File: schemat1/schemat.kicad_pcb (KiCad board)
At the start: 2 copper layers, 100 x 100 mm, 91 parts, among them J1 Light Test Bridge, J2 Power Pins, Q1 BC547, Q2 BC547, Q3 BC547, Q4 BC547, Q5 NMOS, SW1 Player 1, SW2 Player 2, SW3 SW_Push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

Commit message: zmiana elementu C7 na elektrolityczny, aktualizacja w schemacie i na pcb
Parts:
- C7: value 10n -> 100u; footprint Capacitor_THT:C_Disc_D3.4mm_W2.1mm_P2.50mm -> Capacitor_THT:CP_Radial_D6.3mm_P2.50mm
- moved R9 4.45 mm to (33.4, 108.0)
- moved R15 4.25 mm to (33.3, 103.2)
- moved R13 2.55 mm to (33.3, 98.4)
- moved R11 1.85 mm to (33.4, 92.6)
- moved C7 1.77 mm to (41.0, 114.0), turned to 0 degrees
- moved TP9 1.75 mm to (48.0, 117.5)
- moved R8 0.15 mm to (33.4, 87.8)
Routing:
- net Net-(U5-DIS): track 21.0 -> 27.2 mm
- net Net-(Q4-C): track 3.45 -> 5.57 mm
- net Net-(Q3-C): track 3.53 -> 4.85 mm
- net Net-(Q2-C): track 3.45 -> 4.48 mm
- net Net-(Q1-E): track 38.8 -> 38.1 mm
- net Net-(Q1-C): track 3.45 -> 4.02 mm

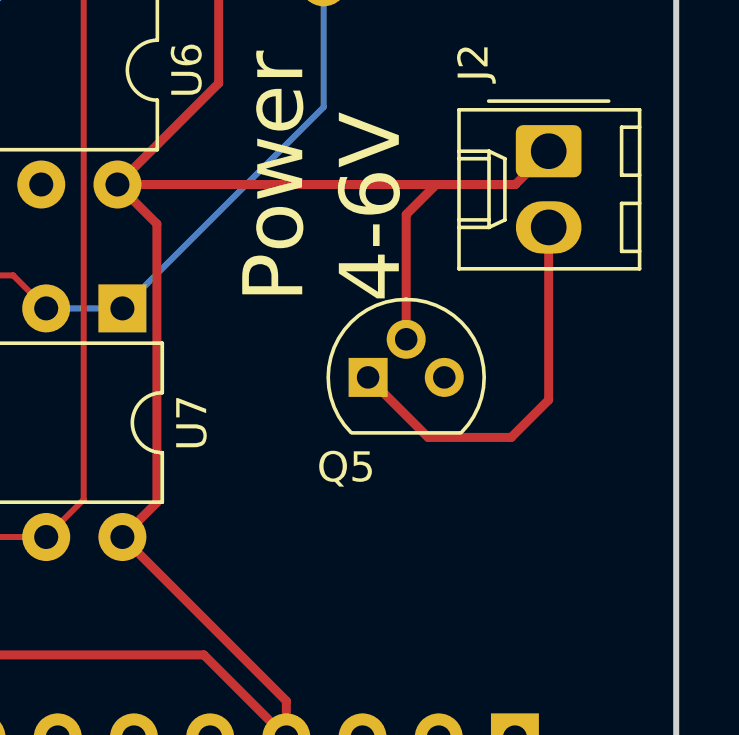
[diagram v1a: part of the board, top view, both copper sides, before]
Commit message: zmiana footprinta tranzystora w układzie zabezpieczającym przed przeciwną polaryzacją
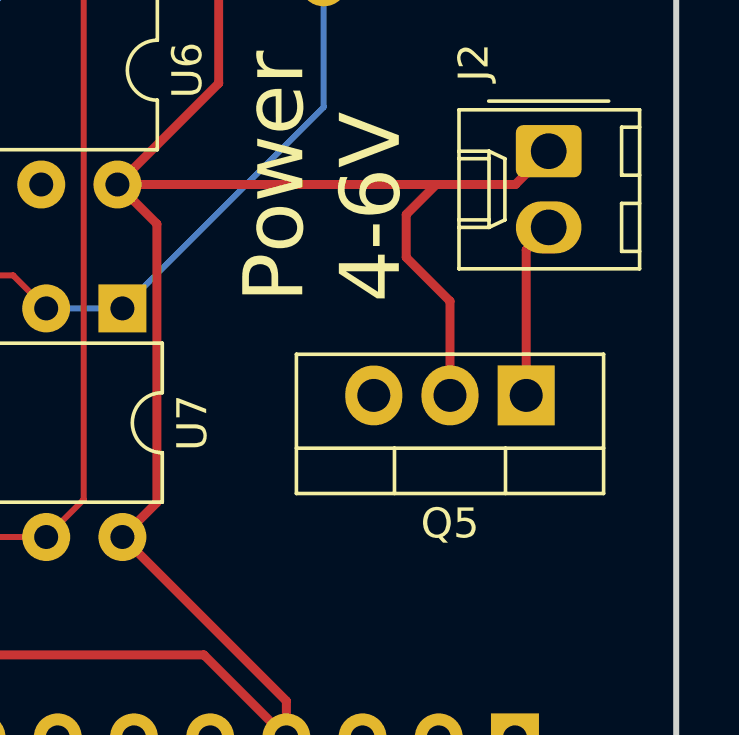
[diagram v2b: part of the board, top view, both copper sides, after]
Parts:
- Q5: footprint Package_TO_SOT_THT:TO-92 -> Package_TO_SOT_THT:TO-220-3_Vertical
- moved Q5 5.30 mm to (115.0, 60.6), turned to 180 degrees
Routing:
- net Net-(J2-Pin_2): track 13.8 -> 6.62 mm
- net +5V: track 369.7 -> 372.2 mm
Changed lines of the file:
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@@
 		)
 	)
-	(footprint "Package_TO_SOT_THT:TO-92"
+	(footprint "Package_TO_SOT_THT:TO-220-3_Vertical"
 		(layer "F.Cu")
-		(at 109.73 60)
-		(descr "TO-92 leads molded, narrow, drill 0.75mm (see NXP sot054_po.pdf)")
-		(tags "to-92 sc-43 sc-43a sot54 PA33 transistor")
+		(at 115 60.6 180)
+		(descr "TO-220-3, Vertical, RM 2.54mm, see https://www.vishay.com/docs/66542/to-220-1.pdf")
+		(tags "TO-220-3 Vertical RM 2.54mm")
 		(property "Reference" "Q5"
-			(at -0.73 3 0)
+			(at 2.54 -4.27 180)
 			(layer "F.SilkS")
 			(effects
@@
 		)
 		(property "Value" "NMOS"
-			(at 1.27 2.79 0)
+			(at 2.54 2.5 180)
 			(layer "F.Fab")
 			(effects
@@
 			)
 		)
-		(property "Footprint" "Package_TO_SOT_THT:TO-92"
-			(at 0 0 0)
+		(property "Footprint" "Package_TO_SOT_THT:TO-220-3_Vertical"
+			(at 0 0 180)
 			(unlocked yes)
 			(layer "F.Fab")
@@
 		)
 		(property "Datasheet" "https://ngspice.sourceforge.io/docs/ngspice-html-manual/manual.xhtml#cha_MOSFETs"
-			(at 0 0 0)
+			(at 0 0 180)
 			(unlocked yes)
 			(layer "F.Fab")
@@
 		)
 		(property "Description" "N-MOSFET transistor, drain/source/gate"
-			(at 0 0 0)
+			(at 0 0 180)
 			(unlocked yes)
 			(layer "F.Fab")
@@
 		)
 		(property "Sim.Device" "NMOS"
-			(at 0 0 0)
+			(at 0 0 180)
 			(unlocked yes)
 			(layer "F.Fab")
@@
 		)
 		(property "Sim.Type" "VDMOS"
-			(at 0 0 0)
+			(at 0 0 180)
 			(unlocked yes)
 			(layer "F.Fab")
@@
 		)
 		(property "Sim.Pins" "1=D 2=G 3=S"
-			(at 0 0 0)
+			(at 0 0 180)
 			(unlocked yes)
 			(layer "F.Fab")
@@
 		(attr through_hole)
 		(fp_line
-			(start -0.53 1.85)
-			(end 3.07 1.85)
+			(start 7.66 -3.27)
+			(end 7.66 1.371)
 			(stroke
 				(width 0.12)
@@
 			(layer "F.SilkS")
 		)
-		(fp_arc
-			(start -0.568478 1.838478)
-			(mid -1.132087 -0.994977)
-			(end 1.27 -2.6)
+		(fp_line
+			(start 4.391 -3.27)
+			(end 4.391 -1.76)
 			(stroke
 				(width 0.12)
@@
 			(layer "F.SilkS")
 		)
-		(fp_arc
-			(start 1.27 -2.6)
-			(mid 3.672087 -0.994977)
-			(end 3.108478 1.838478)
+		(fp_line
+			(start 0.69 -3.27)
+			(end 0.69 -1.76)
 			(stroke
 				(width 0.12)
@@
 		)
 		(fp_line
-			(start -1.46 -2.73)
-			(end -1.46 2.01)
+			(start -2.58 1.371)
+			(end 7.66 1.371)
+			(stroke
+				(width 0.12)
+				(type solid)
+			)
+			(layer "F.SilkS")
+		)
+		(fp_line
+			(start -2.58 -1.76)
+			(end 7.66 -1.76)
+			(stroke
+				(width 0.12)
+				(type solid)
+			)
+			(layer "F.SilkS")
+		)
+		(fp_line
+			(start -2.58 -3.27)
+			(end 7.66 -3.27)
+			(stroke
+				(width 0.12)
+				(type solid)
+			)
+			(layer "F.SilkS")
+		)
+		(fp_line
+			(start -2.58 -3.27)
+			(end -2.58 1.371)
+			(stroke
+				(width 0.12)
+				(type solid)
+			)
+			(layer "F.SilkS")
+		)
+		(fp_line
+			(start 7.79 1.51)
+			(end 7.79 -3.4)
 			(stroke
 				(width 0.05)
@@
 		)
 		(fp_line
-			(start -1.46 -2.73)
-			(end 4 -2.73)
+			(start 7.79 -3.4)
+			(end -2.71 -3.4)
 			(stroke
 				(width 0.05)
@@
 		)
 		(fp_line
-			(start 4 2.01)
-			(end -1.46 2.01)
+			(start -2.71 1.51)
+			(end 7.79 1.51)
 			(stroke
 				(width 0.05)
@@
 		)
 		(fp_line
-			(start 4 2.01)
-			(end 4 -2.73)
+			(start -2.71 -3.4)
+			(end -2.71 1.51)
 			(stroke
 				(width 0.05)
@@
 		)
 		(fp_line
-			(start -0.5 1.75)
-			(end 3 1.75)
+			(start 7.54 1.25)
+			(end 7.54 -3.15)
 			(stroke
 				(width 0.1)
@@
 			(layer "F.Fab")
 		)
-		(fp_arc
-			(start -0.483625 1.753625)
-			(mid -1.021221 -0.949055)
-			(end 1.27 -2.48)
+		(fp_line
+			(start 7.54 -3.15)
+			(end -2.46 -3.15)
 			(stroke
 				(width 0.1)
@@
 			(layer "F.Fab")
 		)
-		(fp_arc
-			(start 1.27 -2.48)
-			(mid 3.561221 -0.949055)
-			(end 3.023625 1.753625)
+		(fp_line
+			(start 4.39 -3.15)
+			(end 4.39 -1.88)
+			(stroke
+				(width 0.1)
+				(type solid)
+			)
+			(layer "F.Fab")
+		)
+		(fp_line
+			(start 0.69 -3.15)
+			(end 0.69 -1.88)
+			(stroke
+				(width 0.1)
+				(type solid)
+			)
+			(layer "F.Fab")
+		)
+		(fp_line
+			(start -2.46 1.25)
+			(end 7.54 1.25)
+			(stroke
+				(width 0.1)
+				(type solid)
+			)
+			(layer "F.Fab")
+		)
+		(fp_line
+			(start -2.46 -1.88)
+			(end 7.54 -1.88)
+			(stroke
+				(width 0.1)
+				(type solid)
+			)
+			(layer "F.Fab")
+		)
+		(fp_line
+			(start -2.46 -3.15)
+			(end -2.46 1.25)
 			(stroke
 				(width 0.1)
@@
 		)
 		(fp_text user "${REFERENCE}"
-			(at 1.27 0 0)
+			(at 2.54 -4.27 180)
 			(layer "F.Fab")
 			(effects
@@
 		)
 		(pad "1" thru_hole rect
-			(at 0 0)
-			(size 1.3 1.3)
-			(drill 0.75)
+			(at 0 0 180)
+			(size 1.905 2)
+			(drill 1.1)
 			(layers "*.Cu" "*.Mask")
 			(remove_unused_layers no)
@@
 			(pintype "passive")
 		)
-		(pad "2" thru_hole circle
-			(at 1.27 -1.27)
-			(size 1.3 1.3)
-			(drill 0.75)
+		(pad "2" thru_hole oval
+			(at 2.54 0 180)
+			(size 1.905 2)
+			(drill 1.1)
 			(layers "*.Cu" "*.Mask")
 			(remove_unused_layers no)
@@
 			(pintype "input")
 		)
-		(pad "3" thru_hole circle
-			(at 2.54 0)
-			(size 1.3 1.3)
-			(drill 0.75)
+		(pad "3" thru_hole oval
+			(at 5.08 0 180)
+			(size 1.905 2)
+			(drill 1.1)
 			(layers "*.Cu" "*.Mask")
 			(remove_unused_layers no)
@@
 			(pintype "passive")
 		)
-		(model "${KICAD8_3DMODEL_DIR}/Package_TO_SOT_THT.3dshapes/TO-92.wrl"
+		(model "${KICAD8_3DMODEL_DIR}/Package_TO_SOT_THT.3dshapes/TO-220-3_Vertical.wrl"
 			(offset
 				(xyz 0 0 0)
@@
 	)
 	(segment
-		(start 111 54.57)
-		(end 112 53.57)
-		(width 0.3)
-		(layer "F.Cu")
-		(net 2)
-	)
-	(segment
-		(start 111 54.57)
-		(end 111 58.73)
-		(width 0.3)
-		(layer "F.Cu")
-		(net 2)
-	)
-	(segment
 		(start 112 53.57)
 		(end 114.64 53.57)
@@
 	)
 	(segment
+		(start 111 54.57)
+		(end 111 56)
+		(width 0.3)
+		(layer "F.Cu")
+		(net 2)
+	)
+	(segment
 		(start 74.68 71.56)
 		(end 79.38 76.26)
@@
 	)
 	(segment
+		(start 112 53.57)
+		(end 111 54.57)
+		(width 0.3)
+		(layer "F.Cu")
+		(net 2)
+	)
+	(segment
 		(start 104.75 50.195)
 		(end 101.375 53.57)
@@
 	)
 	(segment
+		(start 112.46 57.46)
+		(end 112.46 60.6)
+		(width 0.3)
+		(layer "F.Cu")
+		(net 2)
+	)
+	(segment
 		(start 33.34 102.8)
 		(end 33.34 98.4)
@@
 	)
 	(segment
+		(start 111 56)
+		(end 112.46 57.46)
+		(width 0.3)
+		(layer "F.Cu")
+		(net 2)
+	)
+	(segment
 		(start 33.32 103.2)
 		(end 33.32 102.82)
@@
 	)
 	(segment
-		(start 111.73 62)
-		(end 109.73 60)
-		(width 0.3)
-		(layer "F.Cu")
-		(net 109)
-	)
-	(segment
-		(start 115.75 60.75)
-		(end 114.5 62)
-		(width 0.3)
-		(layer "F.Cu")
-		(net 109)
-	)
-	(segment
-		(start 114.5 62)
-		(end 111.73 62)
+		(start 115 60.6)
+		(end 115 55.75)
 		(width 0.3)
 		(layer "F.Cu")
@@
 	)
 	(segment
-		(start 115.75 55)
-		(end 115.75 60.75)
+		(start 115 55.75)
+		(end 115.75 55)
 		(width 0.3)
 		(layer "F.Cu")
